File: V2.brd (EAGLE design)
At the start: 100 x 100 mm, 53 parts, among them IC1 LM2596S, U1 BTS7960B, U2 BTS7960B, U3 BTS7960B, U4 BTS7960B, U5 SN74AHC244DW, U6 MCP2551

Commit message: V2 finished
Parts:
- moved 5VC_JUMPER 0.64 mm to (71.1, 3.81)
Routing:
- net 5V: track 427.7 -> 426.8 mm
- net VIN: vias 20 -> 24
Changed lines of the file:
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@@
 <drawing>
 <settings>
-<setting alwaysvectorfont="yes"/>
+<setting alwaysvectorfont="no"/>
 <setting verticaltext="up"/>
 </settings>
@@
 </layers>
 <board>
-<fusionsync huburn="a.YnVzaW5lc3M6c3VidTEw" projecturn="a.YnVzaW5lc3M6c3VidTEwI0QyMDIwMDMyMjI3NzM1NDM1Ng" f3durn="urn:adsk.wipprod:dm.lineage:HC2YEfjUSyq8PxX8-wVN_g" pcbguid="" lastpulledtime="" lastsyncedchangeguid="" latestrevisionid="b9a7828e-c651-4ab7-ac10-bfd7c7f73334" lastsyncedrevisionid="b9a7828e-c651-4ab7-ac10-bfd7c7f73334" lastboardhashguid="95e5f991-c3a0-b6bd-a15e-587c2ef4ddac" lastpushedtime="2023-06-21T19:56:43Z" linktopcb3d="true"/>
+<fusionsync huburn="a.YnVzaW5lc3M6c3VidTEw" projecturn="a.YnVzaW5lc3M6c3VidTEwI0QyMDIwMDMyMjI3NzM1NDM1Ng" f3durn="urn:adsk.wipprod:dm.lineage:HC2YEfjUSyq8PxX8-wVN_g" pcbguid="" lastpulledtime="" lastsyncedchangeguid="" latestrevisionid="d9669b24-6f8e-4dff-a7c2-f388320820d9" lastsyncedrevisionid="d9669b24-6f8e-4dff-a7c2-f388320820d9" lastboardhashguid="cca6836b-cbc5-9aeb-76d3-4fdc4b80b450" lastpushedtime="2023-06-22T17:46:45Z" linktopcb3d="true"/>
 <plain>
 <wire x1="0" y1="100" x2="0" y2="0" width="0" layer="20"/>
@@
 <hole x="96.52" y="95.885" drill="3.1"/>
 <hole x="96.52" y="3.175" drill="3.1"/>
-<text x="99.06" y="90.805" size="1.27" layer="26" rot="MR0">Swerve Drive AMR Board V2</text>
-<text x="125.095" y="35.56" size="1.27" layer="26" rot="MR0">Designed By:</text>
-<text x="113.665" y="35.56" size="0.8128" layer="30" rot="MR0">Merthan KARAMAN</text>
-<text x="113.665" y="34.29" size="0.8128" layer="30" rot="MR0">Egemen BAŞOL</text>
+<text x="93.98" y="95.25" size="1.27" layer="26" rot="MR0">Swerve Drive AMR Board V2</text>
+<text x="97.79" y="91.44" size="1.27" layer="26" rot="MR0">Designed By:</text>
+<text x="86.36" y="91.44" size="0.8128" layer="30" rot="MR0">Merthan KARAMAN</text>
+<text x="86.36" y="90.17" size="0.8128" layer="30" rot="MR0">Egemen BAŞOL</text>
 <text x="13.97" y="62.865" size="0.8128" layer="25" rot="SR270" align="bottom-center">VIN/GND</text>
 <text x="84.455" y="97.155" size="0.8128" layer="29">Egemen BAŞOL</text>
@@
 <attribute name="PROD_ID" value=" " x="61.595" y="38.1" size="1.778" layer="27" display="off"/>
 </element>
-<element name="5VC_JUMPER" library="SparkFun-Connectors" library_urn="urn:adsk.eagle:library:513" package="1X02" package3d_urn="urn:adsk.eagle:package:38039/1" override_package3d_urn="urn:adsk.eagle:package:39913040/2" override_package_urn="urn:adsk.eagle:footprint:37654/1" value="" x="71.12" y="3.175" smashed="yes">
-<attribute name="NAME" x="72.39" y="5.207" size="0.8128" layer="25" font="vector" ratio="20" rot="R180" align="top-center"/>
-<attribute name="VALUE" x="69.85" y="1.143" size="0.6096" layer="27" font="vector" ratio="20"/>
+<element name="5VC_JUMPER" library="SparkFun-Connectors" library_urn="urn:adsk.eagle:library:513" package="1X02" package3d_urn="urn:adsk.eagle:package:38039/1" override_package3d_urn="urn:adsk.eagle:package:39913040/2" override_package_urn="urn:adsk.eagle:footprint:37654/1" value="" x="71.12" y="3.81" smashed="yes">
+<attribute name="NAME" x="72.39" y="5.842" size="0.8128" layer="25" font="vector" ratio="20" rot="R180" align="top-center"/>
+<attribute name="VALUE" x="69.85" y="1.778" size="0.6096" layer="27" font="vector" ratio="20"/>
 </element>
 <element name="3VC_JUMPER" library="SparkFun-Connectors" library_urn="urn:adsk.eagle:library:513" package="1X02" package3d_urn="urn:adsk.eagle:package:38039/1" override_package3d_urn="urn:adsk.eagle:package:39913040/2" override_package_urn="urn:adsk.eagle:footprint:37654/1" value="" x="65.405" y="3.81" smashed="yes" rot="R180">
@@
 <wire x1="77.84" y1="9.525" x2="77.84" y2="13.6" width="0.6096" layer="1"/>
 <wire x1="77.84" y1="13.6" x2="74.93" y2="16.51" width="0.6096" layer="1"/>
-<wire x1="77.84" y1="9.525" x2="73.66" y2="5.345" width="0.6096" layer="1"/>
-<wire x1="73.66" y1="5.345" x2="73.66" y2="3.175" width="0.6096" layer="1"/>
+<wire x1="77.84" y1="9.525" x2="77.84" y2="8.255" width="0.6096" layer="1"/>
+<wire x1="77.84" y1="8.255" x2="73.66" y2="4.075" width="0.6096" layer="1"/>
+<wire x1="73.66" y1="4.075" x2="73.66" y2="3.81" width="0.6096" layer="1"/>
 <wire x1="81.915" y1="88.685" x2="80.225" y2="86.995" width="1.524" layer="1"/>
 <wire x1="75.825" y1="86.995" x2="74.295" y2="88.525" width="1.524" layer="1"/>
@@
 <wire x1="97.155" y1="51.435" x2="97.155" y2="9.525" width="1.524" layer="1"/>
 <wire x1="97.155" y1="9.525" x2="93.98" y2="6.35" width="1.524" layer="1"/>
-<wire x1="76.835" y1="6.35" x2="73.66" y2="3.175" width="1.524" layer="1"/>
+<wire x1="76.2" y1="6.35" x2="73.66" y2="3.81" width="1.524" layer="1"/>
 <wire x1="92.075" y1="85.09" x2="97.155" y2="80.01" width="1.524" layer="1"/>
-<wire x1="93.98" y1="6.35" x2="76.835" y2="6.35" width="1.524" layer="1"/>
+<wire x1="93.98" y1="6.35" x2="76.2" y2="6.35" width="1.524" layer="1"/>
 <wire x1="55.88" y1="38.54" x2="62.425" y2="45.085" width="0.6096" layer="1"/>
 <wire x1="86.36" y1="45.085" x2="90.17" y2="48.895" width="0.6096" layer="1"/>
@@
 <via x="16.51" y="74.93" extent="1-16" drill="1"/>
 <via x="19.685" y="74.93" extent="1-16" drill="1"/>
+<via x="33.02" y="80.01" extent="1-16" drill="1"/>
+<via x="36.195" y="80.01" extent="1-16" drill="1"/>
+<via x="33.02" y="77.47" extent="1-16" drill="1"/>
+<via x="36.195" y="77.47" extent="1-16" drill="1"/>
 </signal>
 <signal name="N$1">
@@
 <contactref element="5VC_JUMPER" pad="1"/>
 <contactref element="U$1" pad="P$18"/>
-<wire x1="71.12" y1="3.175" x2="69.85" y2="3.175" width="0.6096" layer="1"/>
-<wire x1="69.85" y1="3.175" x2="66.675" y2="6.35" width="0.6096" layer="1"/>
+<wire x1="71.12" y1="3.81" x2="69.215" y2="3.81" width="0.6096" layer="1"/>
+<wire x1="69.215" y1="3.81" x2="66.675" y2="6.35" width="0.6096" layer="1"/>
 <wire x1="66.675" y1="6.35" x2="63.5" y2="6.35" width="0.6096" layer="1"/>
 <wire x1="63.5" y1="6.35" x2="62.865" y2="6.985" width="0.6096" layer="1"/>

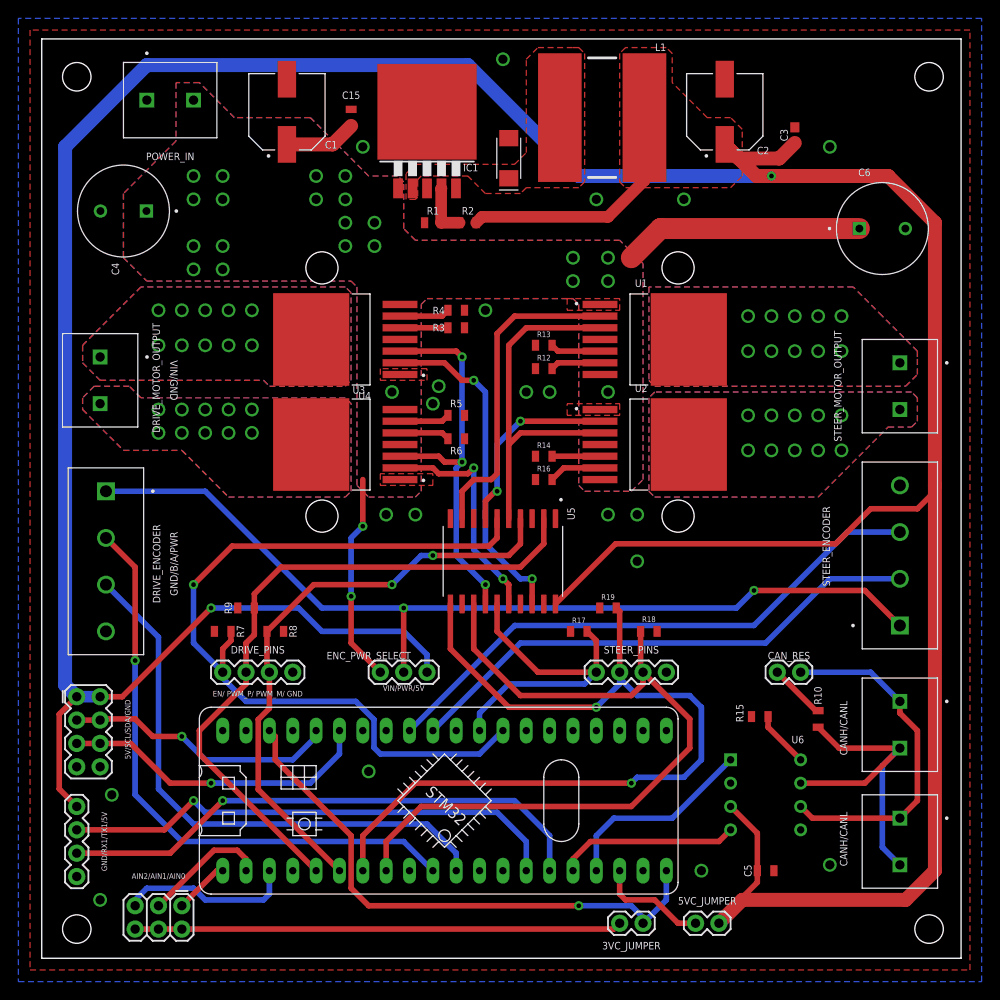
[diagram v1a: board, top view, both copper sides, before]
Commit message: Fixed minor design problems
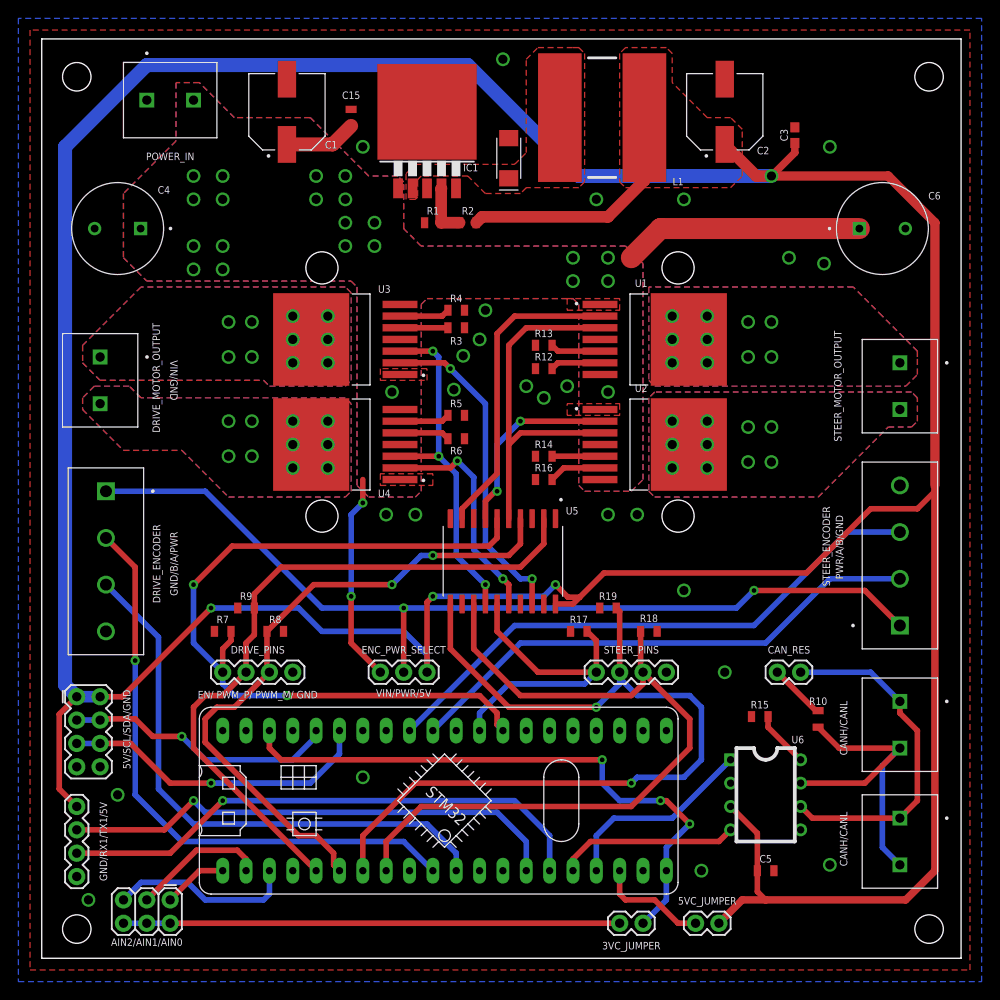
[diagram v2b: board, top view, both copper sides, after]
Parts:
- moved C4 2.01 mm to (8.26, 79.4)
- moved AIN2/AIN1/AIN0 1.42 mm to (14.0, 6.35)
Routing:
- net 5V: track 426.8 -> 444.2 mm, vias 2 -> 4
- net DRIVE_M_M: track 64.6 -> 71.6 mm
- net DRIVE_INH: track 42.5 -> 37.7 mm
- net 3.3VC: track 61.3 -> 65.4 mm, vias 1 -> 3
- net DRIVE_M_EN: track 90.3 -> 87.5 mm, vias 1 -> 2
- net DRIVE_M_P: track 74.3 -> 76.0 mm
- net AIN2: track 19.1 -> 20.3 mm
- net STEER_L_IN: track 34.8 -> 33.7 mm
- net 3.3V: track 53.0 -> 54.0 mm
- net AIN1: track 13.7 -> 14.7 mm
- net AIN0: track 6.02 -> 7.03 mm
- net DRIVE_L_IN: track 36.5 -> 35.8 mm
